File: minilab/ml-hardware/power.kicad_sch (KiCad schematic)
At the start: 4 parts, among them J3 Conn_01x02

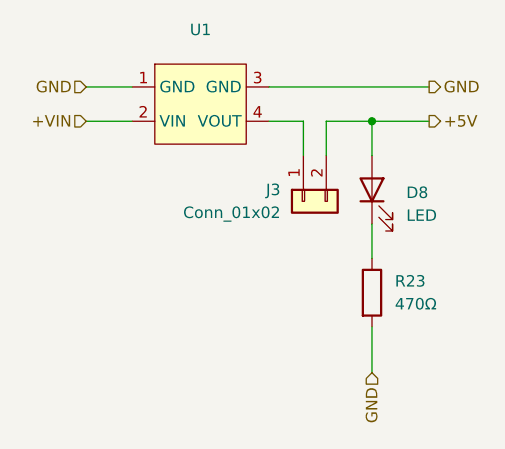
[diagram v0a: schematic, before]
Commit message: minilab: Enforce "pcb/page" hierarchy on schematic
This does not apply (necessarily) to subpages.
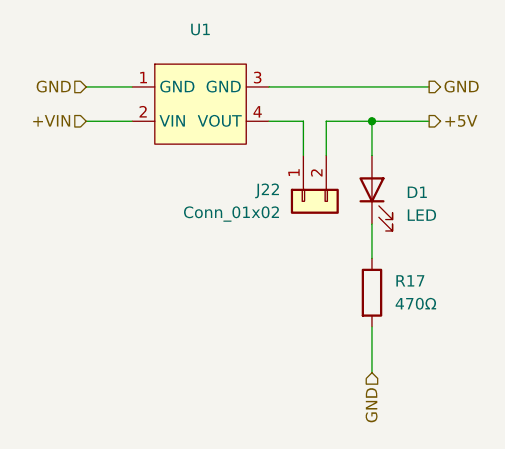
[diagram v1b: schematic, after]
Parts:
- D1: renamed from D8; footprint (none) -> LED_THT:LED_Rectangular_W5.0mm_H2.0mm
- J22: renamed from J3; footprint (none) -> Connector_PinHeader_2.54mm:PinHeader_1x02_P2.54mm_Vertical
- R17: renamed from R23; footprint (none) -> Resistor_THT:R_Axial_DIN0204_L3.6mm_D1.6mm_P5.08mm_Horizontal
- U1: footprint (none) -> Extras:DC-DC_buck
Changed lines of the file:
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@@
 		(dnp no)
 		(fields_autoplaced yes)
-		(property "Reference" "R23"
+		(property "Reference" "R17"
 			(at 176.53 124.4599 0)
 			(effects
@@
 			)
 		)
-		(property "Footprint" ""
+		(property "Footprint" "Resistor_THT:R_Axial_DIN0204_L3.6mm_D1.6mm_P5.08mm_Horizontal"
 			(at 172.212 125.73 90)
 			(effects
@@
 		(instances
 			(project "ml-hardware"
-				(path "/edb8a0df-1def-48df-b494-4a6b89ce8f9c/6c358c04-6120-418c-ae6f-89bc5b99575c"
-					(reference "R23")
+				(path "/edb8a0df-1def-48df-b494-4a6b89ce8f9c/d397cdb8-1135-4612-aff9-bdf84d932419/8be39316-7f63-43eb-b9fa-7cc8c702fc5c"
+					(reference "R17")
 					(unit 1)
 				)
@@
 		(dnp no)
 		(fields_autoplaced yes)
-		(property "Reference" "D8"
+		(property "Reference" "D1"
 			(at 177.8 114.6174 90)
 			(effects
@@
 			)
 		)
-		(property "Footprint" ""
+		(property "Footprint" "LED_THT:LED_Rectangular_W5.0mm_H2.0mm"
 			(at 173.99 114.3 0)
 			(effects
@@
 		)
 		(instances
-			(project ""
-				(path "/edb8a0df-1def-48df-b494-4a6b89ce8f9c/6c358c04-6120-418c-ae6f-89bc5b99575c"
-					(reference "D8")
+			(project "ml-hardware"
+				(path "/edb8a0df-1def-48df-b494-4a6b89ce8f9c/d397cdb8-1135-4612-aff9-bdf84d932419/8be39316-7f63-43eb-b9fa-7cc8c702fc5c"
+					(reference "D1")
 					(unit 1)
 				)
@@
 			)
 		)
-		(property "Footprint" ""
+		(property "Footprint" "Extras:DC-DC_buck"
 			(at 154.94 99.06 0)
 			(effects
@@
 		)
 		(instances
-			(project ""
-				(path "/edb8a0df-1def-48df-b494-4a6b89ce8f9c/6c358c04-6120-418c-ae6f-89bc5b99575c"
+			(project "ml-hardware"
+				(path "/edb8a0df-1def-48df-b494-4a6b89ce8f9c/d397cdb8-1135-4612-aff9-bdf84d932419/8be39316-7f63-43eb-b9fa-7cc8c702fc5c"
 					(reference "U1")
 					(unit 1)
@@
 		(on_board yes)
 		(dnp no)
-		(property "Reference" "J3"
+		(property "Reference" "J22"
 			(at 163.83 114.2999 90)
 			(effects
@@
 			)
 		)
-		(property "Footprint" ""
+		(property "Footprint" "Connector_PinHeader_2.54mm:PinHeader_1x02_P2.54mm_Vertical"
 			(at 166.37 115.57 0)
 			(effects
@@
 		)
 		(instances
-			(project ""
-				(path "/edb8a0df-1def-48df-b494-4a6b89ce8f9c/6c358c04-6120-418c-ae6f-89bc5b99575c"
-					(reference "J3")
-					(unit 1)
-				)
+			(project "ml-hardware"
+				(path "/edb8a0df-1def-48df-b494-4a6b89ce8f9c/d397cdb8-1135-4612-aff9-bdf84d932419/8be39316-7f63-43eb-b9fa-7cc8c702fc5c"
+					(reference "J22")
+					(unit 1)
+				)
